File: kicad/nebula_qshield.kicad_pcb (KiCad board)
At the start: 4 copper layers, 100 x 100 mm, 153 parts, among them J1 J1, J10 J10, J11 J11, J12 J12, J13 J13, J14 J14, J15 J15, J16 J16, J17 J17, J18 J18, J19 J19, J2 J2, J20 J20, J21 J21, J3 J3, J4 J4, J5 J5, J6 J6, J7 J7, J8 J8, J9 J9, K1 HF46F-12-HS1, K2 HF46F-12-HS1, Q1 IRLZ44NPBF, Q2 IRLZ44NPBF, Q3 2N7002, Q4 2N7002, Q5 IRLZ44NPBF, SW1 RESET, T1 Transformer_SP_2S, T2 Transformer_SP_2S, T3 Transformer_SP_2S, U1 TPS54302DDCR, U10 MCP6002, U11 MCP6002, U12 SN6501, U13 AMC1301, U14 HX711, U15 MAX485ESA, U16 PC817X2NIP, U17 IR2104SPBF, U18 PC817X1NIP, U19 PC817X1NIP, U2 AMS1117-3.3, U20 MCP6002, U21 ISO1541, U3 TPS3823-33DBVR, U4 MCP6002, U5 SN6501, U6 AMC1301, U7 MCP6002, U8 SN6501, U9 AMC1301

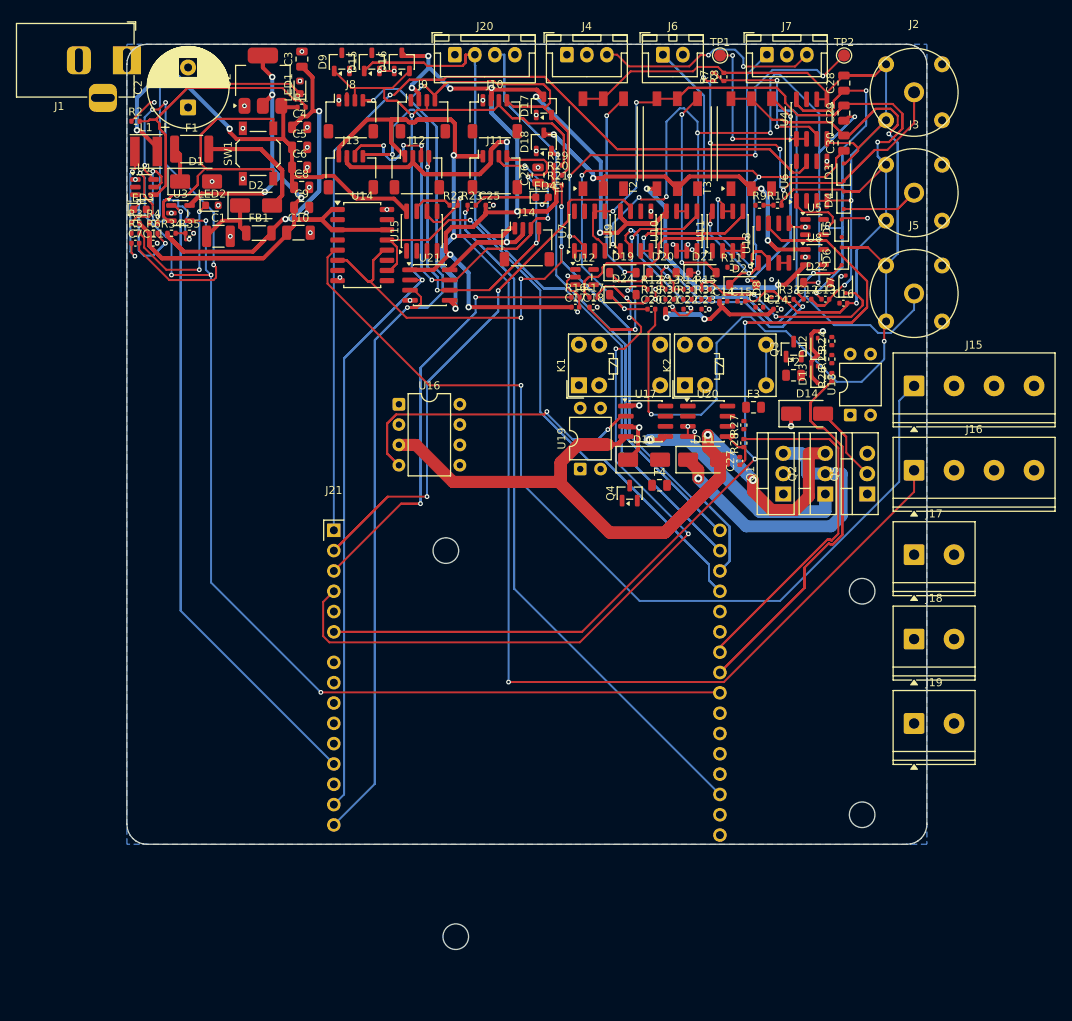
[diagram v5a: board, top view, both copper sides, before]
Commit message: WIP: apply UNO Q re-architecture board changes
- Replace J21 with Arduino_UNO_Q_Shield footprint at (5.08, 35.56)
- Remap I2C_SDA/I2C_SCL to pins 31/32 (D20/D21)
- Reserve A4/A5 (pins 13/14) for CO2_ADC/DO_ADC
- Add R36/R37 4.7k pull-ups to /3V3_RAIL
- Relocate D10, D11, F4, K1, K2, Q4, U16, U17, U19, U20 per plan
- Add Edge.Cuts slots for USB-C, power button, power jack
- Add Eco1.User keepout markers for JCTL, SPI2, QWIIC, USB-C/PMIC
- Add local R_0603_1608Metric footprint
- ERC: 0 violations; DRC: 1108 violations due to placement conflicts

The 19 components that collide with the J21 courtyard (not the 10
from the plan) prevent DRC=0; see UNO_Q_rearchitecture_report.md

Co-Authored-By: Devin AI <158243242+devin-ai-integration[bot]@users.noreply.github.com>
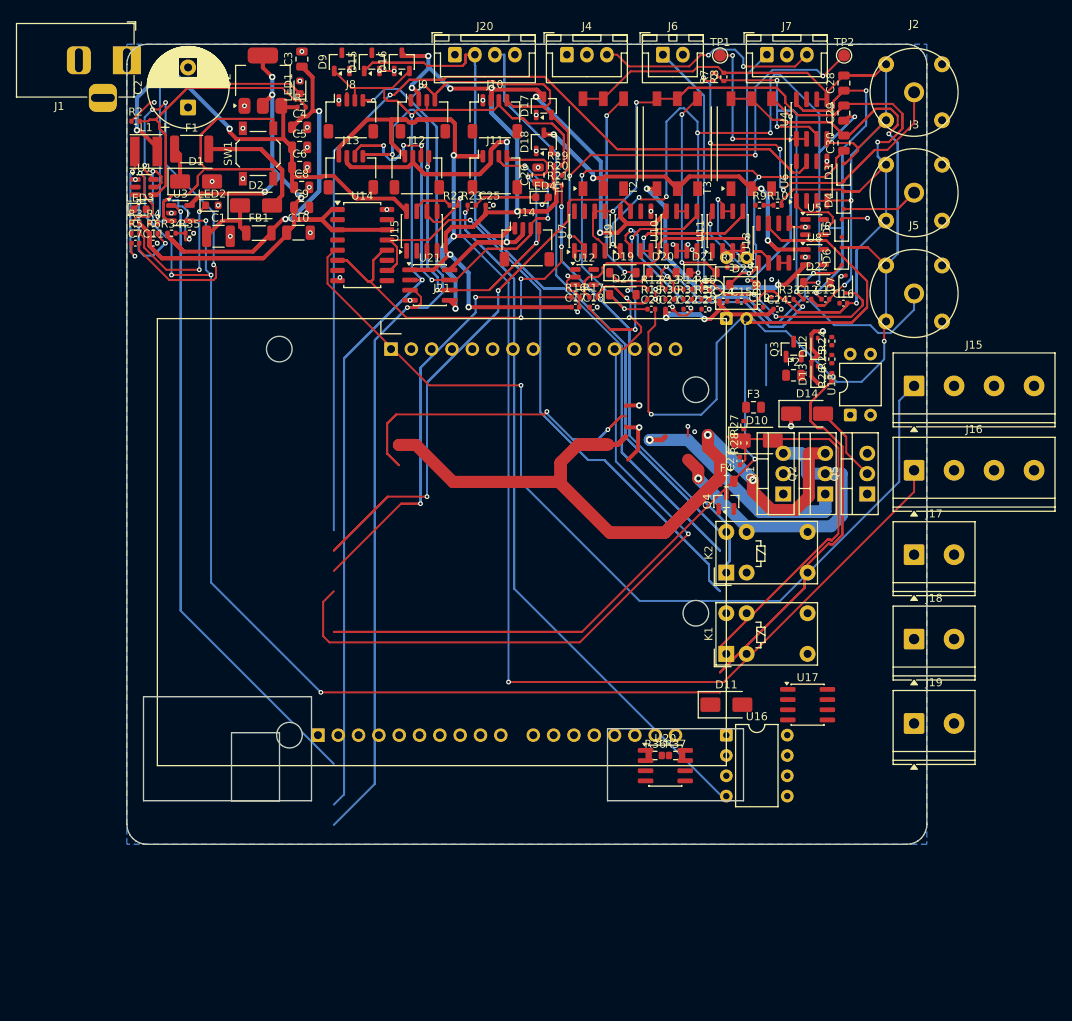
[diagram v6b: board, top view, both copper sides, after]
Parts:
- added R36: 4.7k, nebula_footprints:R_0603_1608Metric, F.Cu at (66.0, 88.9)
- added R37: 4.7k, nebula_footprints:R_0603_1608Metric, F.Cu at (68.6, 88.9)
- J21: value J21 -> Arduino UNO Q Shield; footprint Arduino_UNO_Shield_2x20 -> nebula_footprints:Arduino_UNO_Q_Shield
- moved U16 58.2 mm to (74.9, 86.4)
- moved U20 43.4 mm to (67.3, 90.2)
- moved U17 40.8 mm to (85.1, 82.5)
- moved K1 38.3 mm to (74.9, 76.2)
- moved J21 32.7 mm to (5.08, 35.6)
- moved D11 30.8 mm to (74.9, 82.5)
- moved U19 26.2 mm to (74.9, 34.3)
- moved K2 24.0 mm to (74.9, 66.0)
- moved D10 14.3 mm to (78.7, 49.5)
- moved Q4 12.1 mm to (74.9, 57.1)
- moved F4 8.37 mm to (74.9, 54.6)
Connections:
- J21 pad 1: /PH_ADC -> (no net)
- J21 pad 10: /5V_RAIL -> /ORP_ADC
- J21 pad 11: /3V3_RAIL -> /TEMP_ADC
- J21 pad 12: /MCU_NRST -> /HUM_ADC
- J21 pad 13: unconnected-(J21-IOREF-Pad13) -> /CO2_ADC
- J21 pad 14: /I2C_SDA -> /DO_ADC
- J21 pad 15: /I2C_SCL -> /HMI_RX
- J21 pad 2: /ORP_ADC -> (no net)
- J21 pad 25: /HMI_RX -> (no net)
- J21 pad 26: /HMI_TX -> (no net)
- J21 pad 27: /HX711_DOUT -> (no net)
- J21 pad 28: /HX711_SCK -> /LED_STATUS
- J21 pad 29: /PUMP_DIR -> GND
- J21 pad 3: /TEMP_ADC -> /MCU_NRST
- J21 pad 30: /PUMP_PWM -> (no net)
- J21 pad 31: /CO2_PWM -> /I2C_SDA
- J21 pad 32: /CO2_SOL_CTL -> /I2C_SCL
- J21 pad 4: /HUM_ADC -> /3V3_RAIL
- J21 pad 5: /CO2_ADC -> /5V_RAIL
- J21 pad 6: /DO_ADC -> GND
- J21 pad 7: /12V_RAIL -> GND
- J21 pad 8: GND -> /12V_RAIL
- J21 pad 9: GND -> /PH_ADC
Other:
- outline, holes or cut-outs redrawn
- board text added: "JCTL_keepout"
- board text added: "QWIIC_keepout"
- board text added: "SPI2_keepout"
- board text added: "USB_C PMIC_keepout"

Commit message: feat(re-arch): 100x120 mm UNO Q shield baseline with DRC-0 error level
- Resize board outline to 100 mm x 120 mm with rounded corners and
  Edge.Cuts cutouts for UNO Q USB-C, power button, JCTL, SPI2/Qwiic access.
- Replace J21 with Arduino_UNO_Q_Shield footprint at (5.08, 35.56) mm.
- Remap I2C_SDA/I2C_SCL to pins 31/32 (D20/D21); A4/A5 kept for CO2_ADC/DO_ADC.
- Add physical 4.7k pull-ups R36/R37 tied to 3V3 next to D20/D21.
- Relocate K1/K2/U16/U17/U19/U20/D10/D11/Q4/F4 into the new board area.
- Add Eco1.User keepout markers for the connector keepout zones.
- DRC severity-error: 0 violations (365 unconnected items remain for routing).
- ERC: 0 violations.
- Include helper scripts: prep_100x120_text.py, compute_repack.py,
  apply_positions.py, refill_zones.py.

NOTE: hmi_connectors.kicad_sch still uses the old 31-pin J21 symbol;
      update to the 32-pin corrected symbol and add I2C pull-up symbols
      in a follow-up commit.
Co-Authored-By: Devin AI <158243242+devin-ai-integration[bot]@users.noreply.github.com>
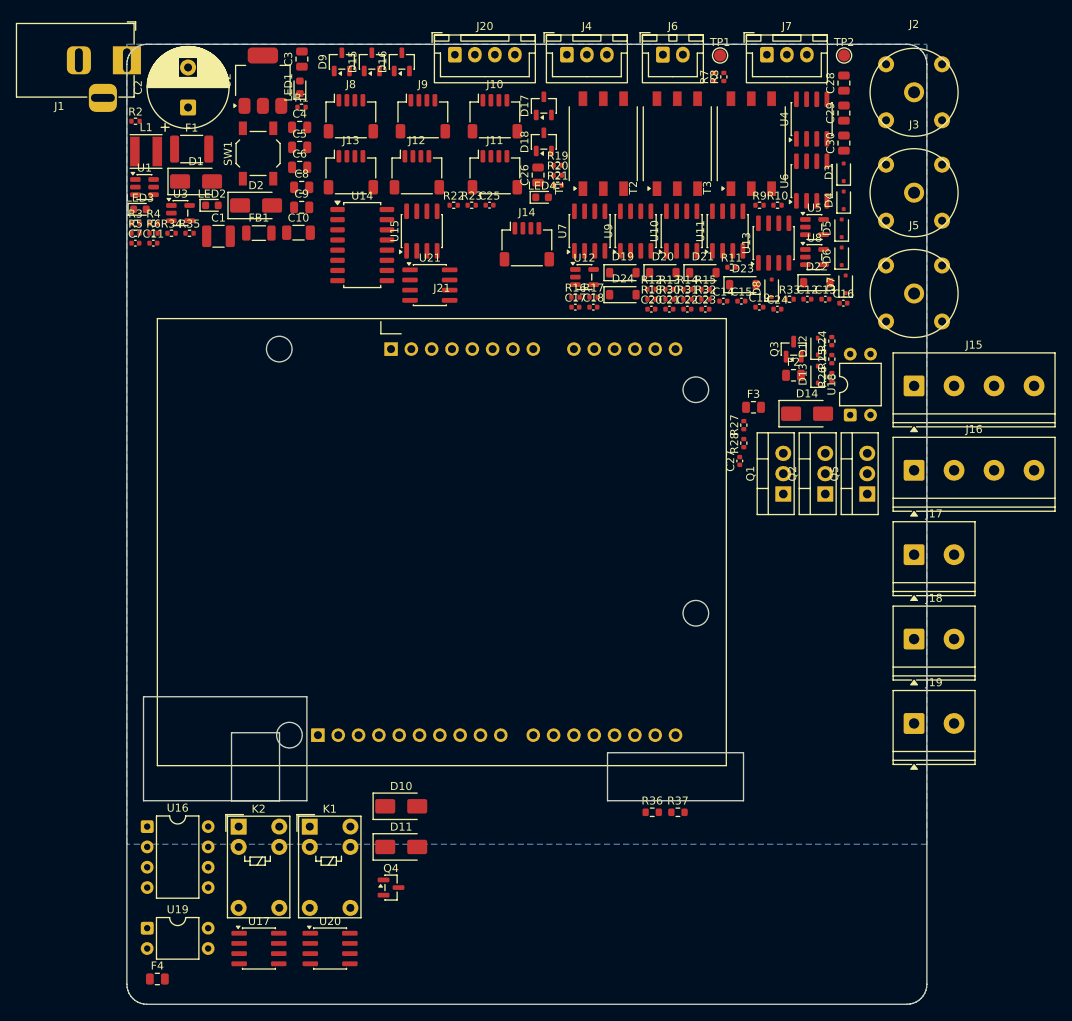
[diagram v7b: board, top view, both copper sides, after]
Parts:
- moved U19 105.1 mm to (2.54, 110.5), turned to 0 degrees
- moved F4 94.5 mm to (3.81, 116.8)
- moved U17 75.0 mm to (16.5, 113.0)
- moved U16 73.3 mm to (2.54, 97.8)
- moved K2 68.7 mm to (14.0, 97.8), turned to 0 degrees
- moved Q4 63.9 mm to (33.0, 105.4), turned to 0 degrees
- moved D10 63.8 mm to (34.3, 95.2)
- moved K1 56.4 mm to (22.9, 97.8), turned to 0 degrees
- moved U20 47.7 mm to (25.4, 113.0)
- moved D11 44.4 mm to (34.3, 100.3)
- moved R36 7.11 mm to (65.7, 96.0)
- moved R37 7.11 mm to (68.9, 96.0)
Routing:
- net /3V3_RAIL: track 315.0 -> 0.00 mm, vias 15 -> 0
- net /I2C_SCL: track 281.5 -> 0.00 mm, vias 3 -> 0
- net /I2C_SDA: track 267.1 -> 0.00 mm, vias 2 -> 0
- net /DO_ADC: track 198.1 -> 0.00 mm, vias 2 -> 0
- net /HMI_TX: track 192.8 -> 0.00 mm
- net /PH_ADC: track 184.2 -> 0.00 mm, vias 1 -> 0
- net /Analog Acquisition/GND_ISO_ORP: track 182.0 -> 0.00 mm, vias 4 -> 0
- net /HX711_DOUT: track 168.3 -> 0.00 mm, vias 4 -> 0
- net /Analog Acquisition/GND_ISO_DO: track 163.8 -> 0.00 mm, vias 3 -> 0
- net /PGND: track 147.0 -> 0.00 mm, vias 2 -> 0
- net /LED_STATUS: track 145.6 -> 0.00 mm, vias 1 -> 0
- net /MCU_WDI: track 145.1 -> 0.00 mm, vias 5 -> 0
- net /HMI_RX: track 141.3 -> 0.00 mm, vias 1 -> 0
- net /Digital & I2C/RS485_A: track 138.6 -> 0.00 mm, vias 2 -> 0
- net /HX711_SCK: track 133.0 -> 0.00 mm, vias 1 -> 0
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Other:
- board size 100 x 100 mm -> 100 x 120 mm
